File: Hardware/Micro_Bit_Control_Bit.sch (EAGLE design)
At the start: 51 parts, among them J1 Pokehome, J2 Pokehome, J3 Pokehome, J4 Pokehome, J5 Pokehome, J6 Pokehome, J7 Pokehome, J8 Pokehome, J9 QWIIC_RA, U2 micro:bit

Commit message: library thing - control bit text device now in SFE aethetics
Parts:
- U$4, U$5: device Micro_Bit_Parts:LOGO-CONTROLBIT -> SparkFun-Aesthetics:LOGO-CONTROLBIT
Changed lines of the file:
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@@
 <part name="FD4" library="SparkFun-Aesthetics" deviceset="FIDUCIAL" device="UFIDUCIAL"/>
 <part name="U2" library="SparkFun-Connectors" deviceset="MICRO:BIT*?" device="_RA" value="micro:bit"/>
-<part name="U$4" library="Micro_Bit_Parts" deviceset="LOGO-CONTROLBIT" device=""/>
-<part name="U$5" library="Micro_Bit_Parts" deviceset="LOGO-CONTROLBIT" device=""/>
+<part name="U$4" library="SparkFun-Aesthetics" deviceset="LOGO-CONTROLBIT" device=""/>
+<part name="U$5" library="SparkFun-Aesthetics" deviceset="LOGO-CONTROLBIT" device=""/>
 <part name="J9" library="SparkFun-Connectors" deviceset="QWIIC_CONNECTOR" device="JS-1MM" value="QWIIC_RA"/>
 <part name="SUPPLY7" library="SparkFun-PowerSymbols" deviceset="3.3V" device=""/>

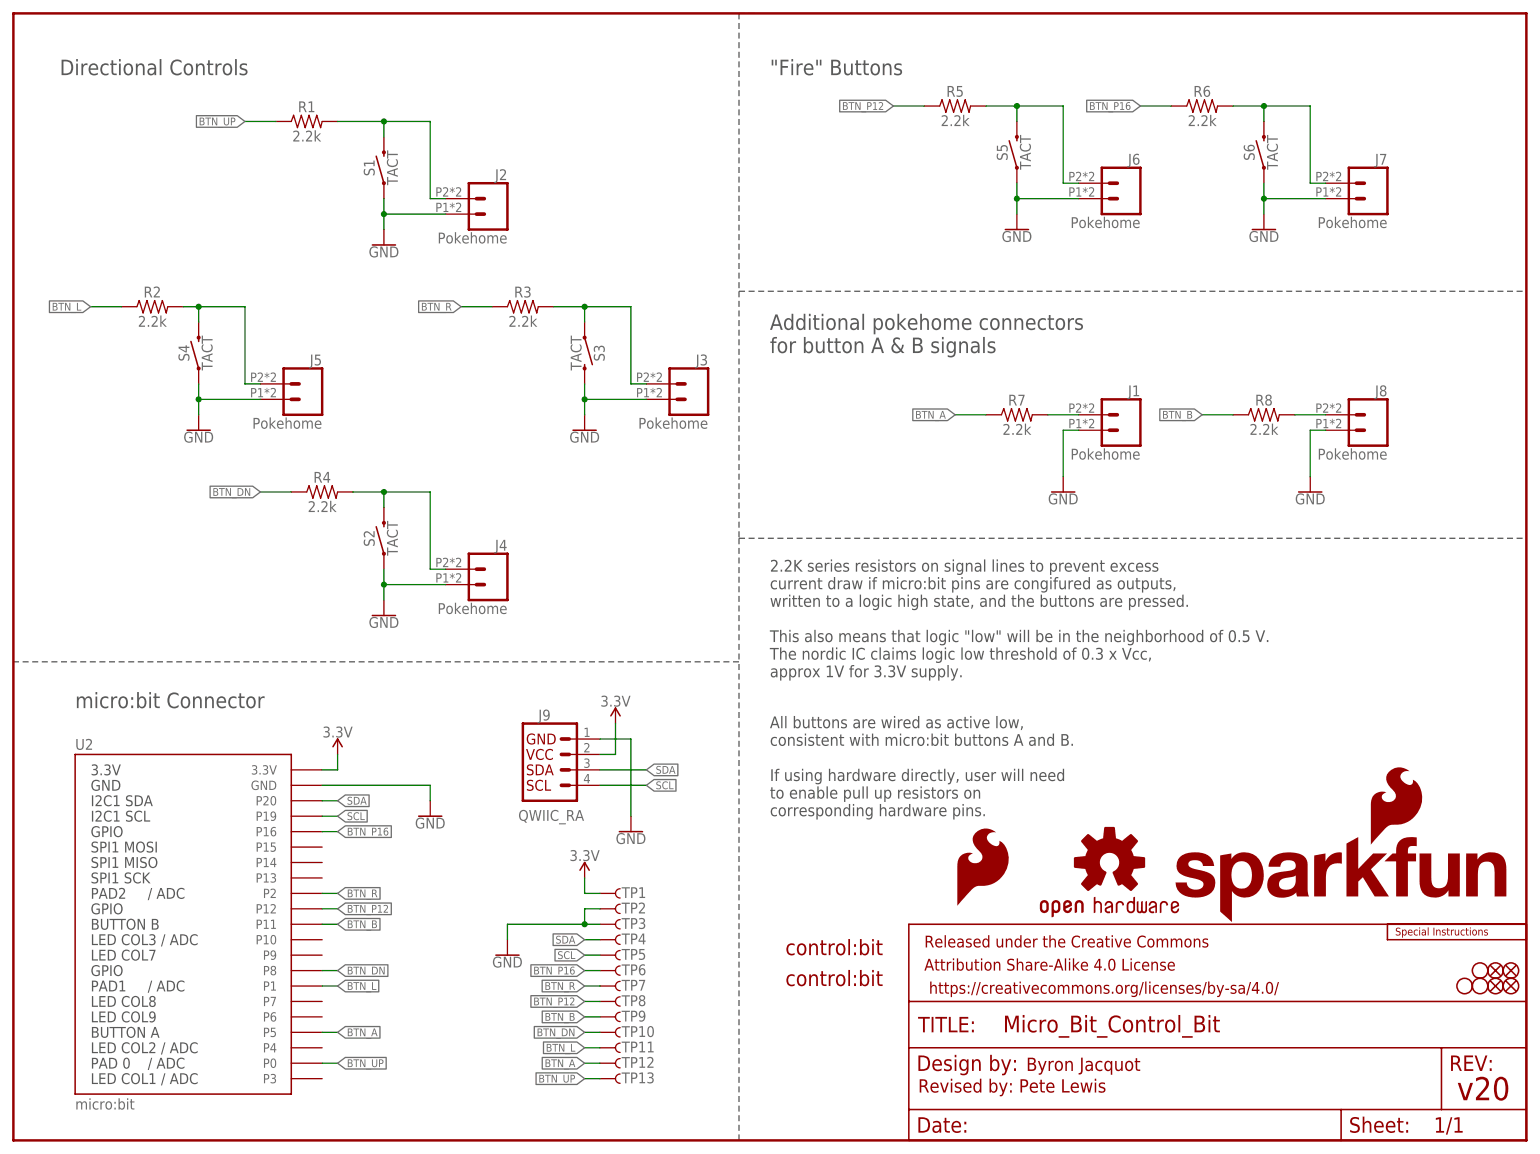
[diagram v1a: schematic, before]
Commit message: sch cleanup and vcc range
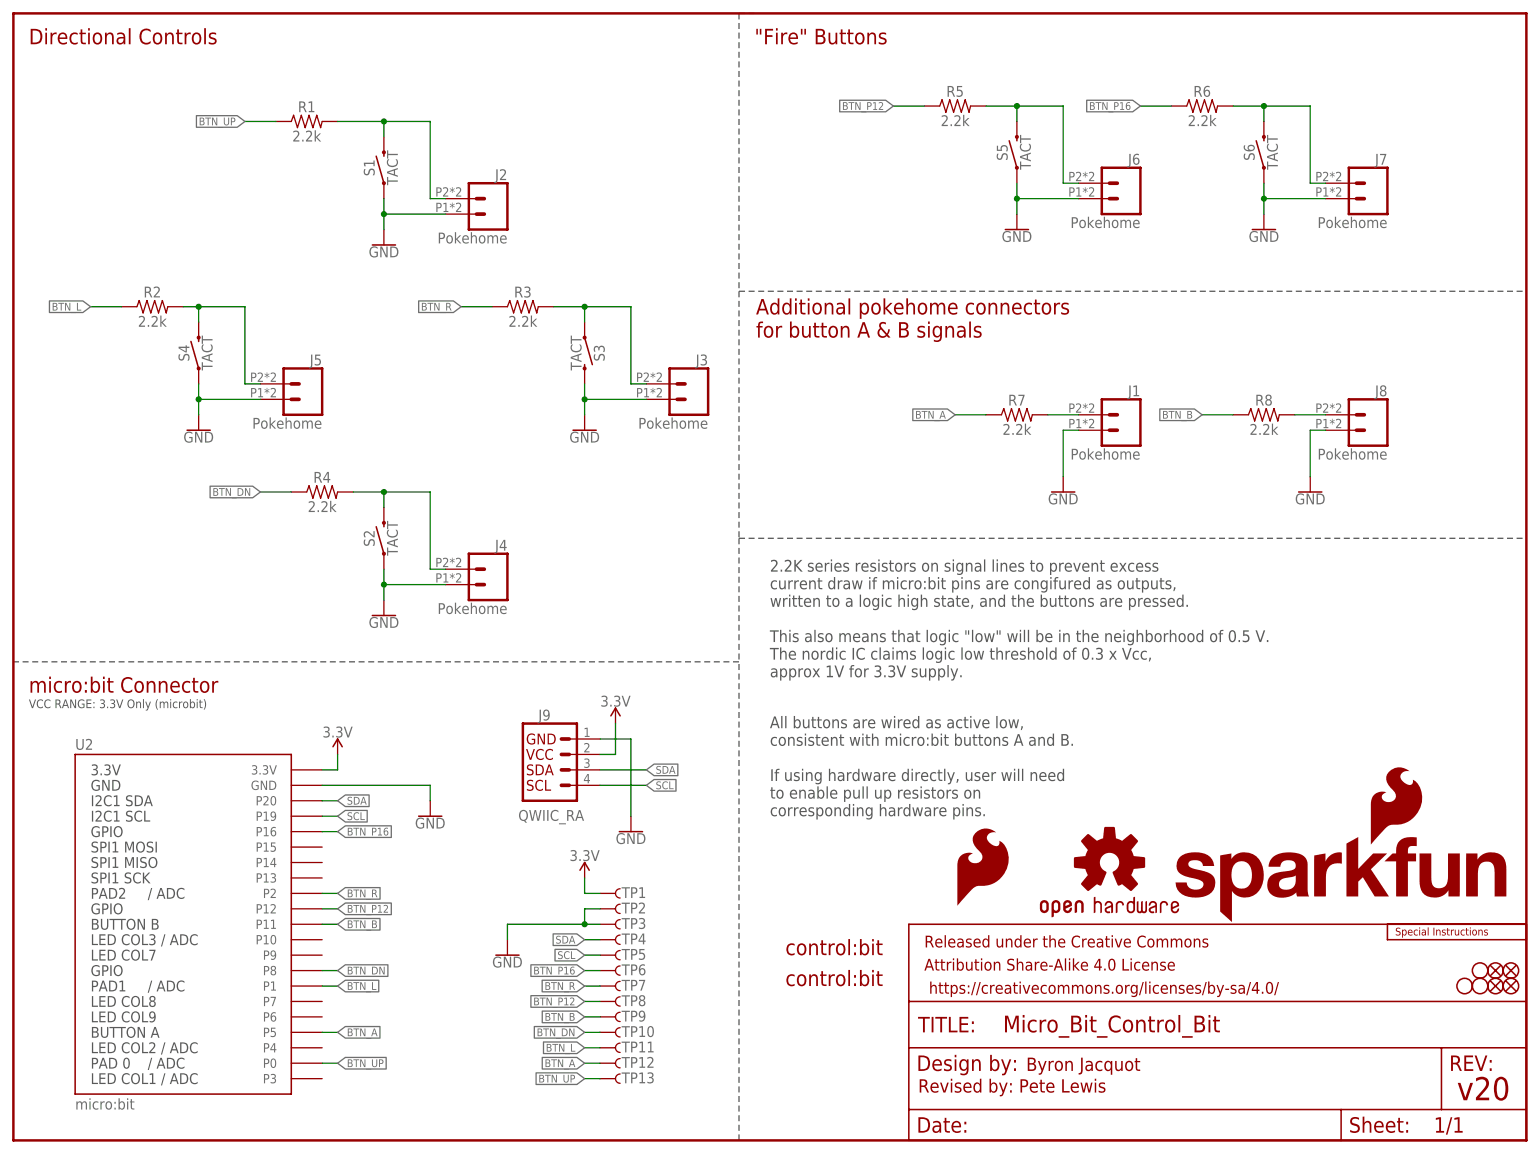
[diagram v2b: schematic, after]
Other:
- note added: "VCC RANGE: 3.3V Only (microbit)"
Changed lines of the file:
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@@
 The nordic IC claims logic low threshold of 0.3 x Vcc,
 approx 1V for 3.3V supply.</text>
-<text x="124.46" y="129.54" size="2.54" layer="97" font="vector">Additional pokehome connectors
+<text x="122.174" y="132.08" size="2.54" layer="94" font="vector">Additional pokehome connectors
 for button A &amp; B signals</text>
-<text x="7.62" y="175.26" size="2.54" layer="97" font="vector">Directional Controls</text>
-<text x="124.46" y="175.26" size="2.54" layer="97" font="vector">"Fire" Buttons</text>
+<text x="2.54" y="180.34" size="2.54" layer="94" font="vector">Directional Controls</text>
+<text x="121.92" y="180.34" size="2.54" layer="94" font="vector">"Fire" Buttons</text>
 <wire x1="121.92" y1="185.42" x2="119.38" y2="185.42" width="0.1524" layer="97" style="shortdash"/>
 <wire x1="119.38" y1="185.42" x2="119.38" y2="139.7" width="0.1524" layer="97" style="shortdash"/>
@@
 <wire x1="119.38" y1="99.06" x2="248.92" y2="99.06" width="0.1524" layer="97" style="shortdash"/>
 <wire x1="119.38" y1="0" x2="119.38" y2="78.74" width="0.1524" layer="97" style="shortdash"/>
-<text x="10.16" y="71.12" size="2.54" layer="97" font="vector">micro:bit Connector</text>
+<text x="2.54" y="73.66" size="2.54" layer="94" font="vector">micro:bit Connector</text>
 <text x="148.844" y="7.874" size="2.1844" layer="94" font="vector">Revised by: Pete Lewis</text>
+<text x="2.54" y="71.12" size="1.4224" layer="97" font="vector">VCC RANGE: 3.3V Only (microbit)</text>
 </plain>
 <instances>

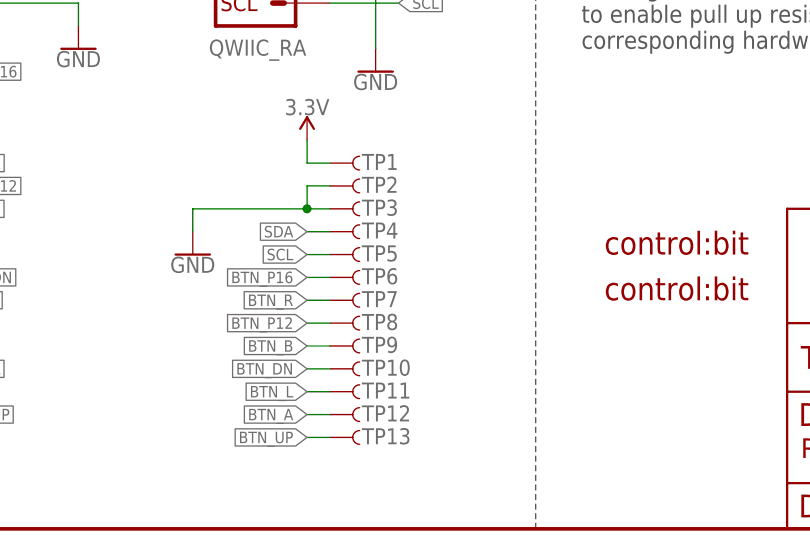
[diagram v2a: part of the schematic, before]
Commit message: bumped test ppoints to larger size
also rearragned VCC pin over so it wasn't right next to GND, to help avoid accidental jumpers between VCC and GND.
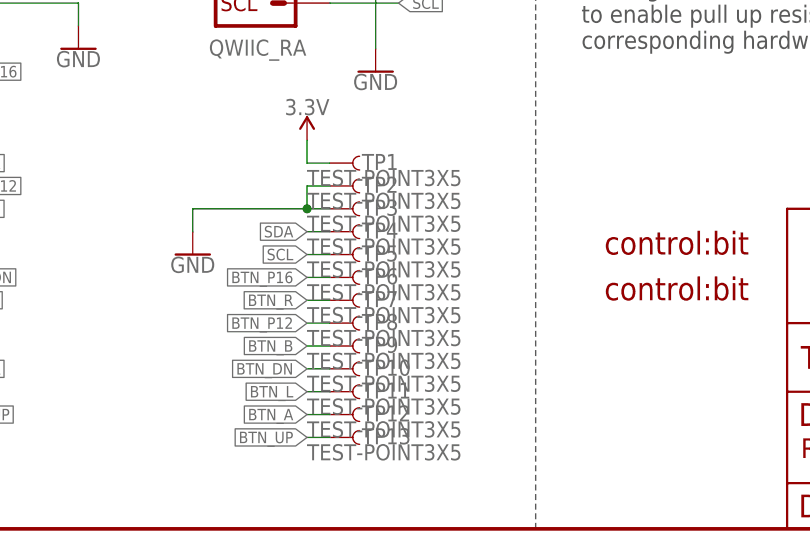
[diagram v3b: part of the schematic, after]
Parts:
- TP1, TP10, TP11, TP12, TP13, TP2, TP3, TP4, TP5, TP6, TP7, TP8, TP9: value TEST-POINT3 -> TEST-POINT3X5; device SparkFun-Connectors:TEST-POINT3 -> SparkFun-Connectors:TEST-POINT3X5
